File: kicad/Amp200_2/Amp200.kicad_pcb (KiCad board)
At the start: 2 copper layers, 26.2 x 21.9 mm, 38 parts, among them J1 Conn, J10 Conn, J2 Conn, J3 Conn, J5 Conn, J6 Conn, J7 Conn, J8 Conn, J9 Conn, U2 NCP1117-3.3

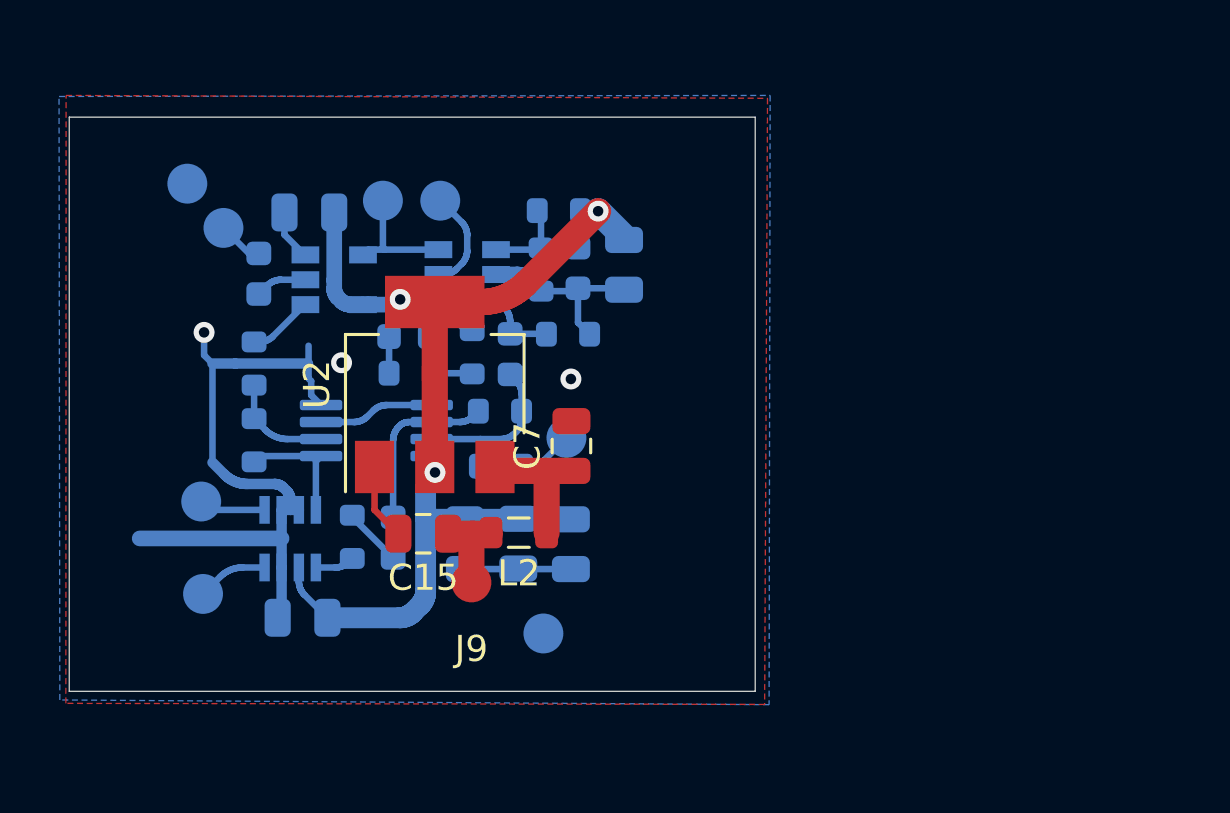
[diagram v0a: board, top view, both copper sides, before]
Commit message: изменено:      kicad/Amp200_2/Amp200-cache.lib 	изменено:      kicad/Amp200_2/Amp200.kicad_pcb 	изменено:      kicad/Amp200_2/Amp200.kicad_pcb-bak 	изменено:      kicad/Amp200_2/Amp200.sch 	изменено:      kicad/Amp200_2/Amp200.sch-bak 	изменено:      kicad/Amp200_2/fp-info-cache 	изменено:      kicad/Anemometr_200_F303/fp-info-cache 	изменено:      stm32cubeide/Anemometer/Release/makefile 	изменено:      stm32cubeide/Anemometer_200_F303/Anemometer_200_F303.ioc 	изменено:      stm32cubeide/Anemometer_200_F303/Core/Inc/main.h 	изменено:      stm32cubeide/Anemometer_200_F303/Core/Inc/stm32f3xx_it.h 	изменено:      stm32cubeide/Anemometer_200_F303/Core/Src/main.c 	изменено:      stm32cubeide/Anemometer_200_F303/Core/Src/stm32f3xx_hal_msp.c 	изменено:      stm32cubeide/Anemometer_200_F303/Core/Src/stm32f3xx_it.c 	изменено:      stm32cubeide/Anemometer_200_F303/Debug/Anemometer_200_F303.bin 	изменено:      stm32cubeide/Anemometer_200_F303/Debug/Anemometer_200_F303.elf 	изменено:      stm32cubeide/Anemometer_200_F303/Debug/Anemometer_200_F303.list 	изменено:      stm32cubeide/Anemometer_200_F303/Debug/Anemometer_200_F303.map 	изменено:      stm32cubeide/Anemometer_200_F303/Debug/Core/Src/main.o 	изменено:      stm32cubeide/Anemometer_200_F303/Debug/Core/Src/main.su 	изменено:      stm32cubeide/Anemometer_200_F303/Debug/Core/Src/stm32f3xx_hal_msp.o 	изменено:      stm32cubeide/Anemometer_200_F303/Debug/Core/Src/stm32f3xx_hal_msp.su 	изменено:      stm32cubeide/Anemometer_200_F303/Debug/Core/Src/stm32f3xx_it.o 	изменено:      stm32cubeide/Anemometer_200_F303/Debug/Core/Src/stm32f3xx_it.su
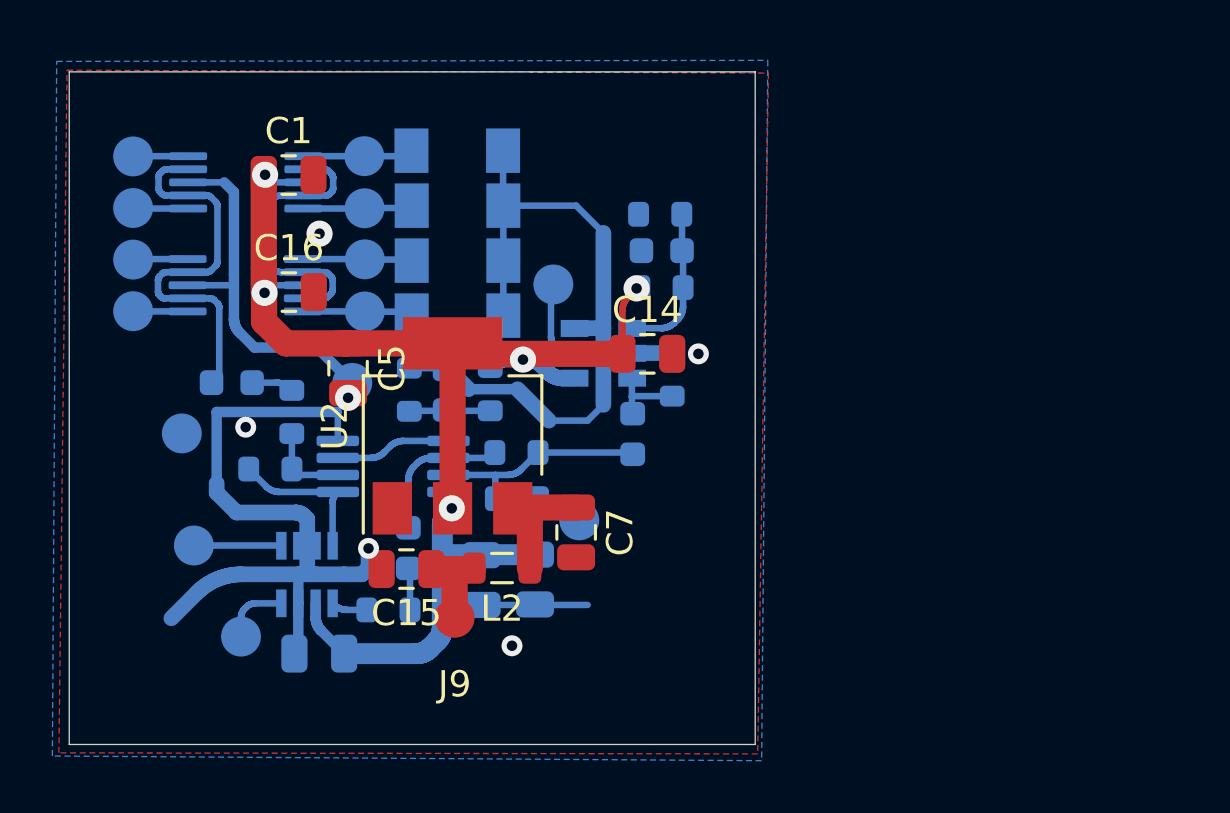
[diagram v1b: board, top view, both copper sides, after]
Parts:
- added C9: 1.5n, Capacitor_SMD:C_0603_1608Metric, B.Cu at (29.1, 47.2)
- added D4: BZ55C2V7, Diode_SMD:D_MiniMELF, B.Cu at (37.7, 44.6)
- added D6: BZ55C2V7, Diode_SMD:D_MiniMELF, B.Cu at (37.7, 40.4)
- added D7: BZ55C2V7, Diode_SMD:D_MiniMELF, B.Cu at (37.7, 38.3)
- added J11: Conn, My-library:SMD-CONN, B.Cu at (34.2, 42.5)
- added J12: Conn, My-library:SMD-CONN, B.Cu at (25.3, 42.5)
- added J13: Conn, My-library:SMD-CONN, B.Cu at (34.2, 40.5)
- added J14: Conn, My-library:SMD-CONN, B.Cu at (25.3, 40.5)
- added J15: Conn, My-library:SMD-CONN, B.Cu at (34.2, 38.5)
- added J16: Conn, My-library:SMD-CONN, B.Cu at (25.3, 38.5)
- added U1: TS5A23159DGS, Package_SO:VSSOP-10_3x3mm_P0.5mm, B.Cu at (29.6, 43.4)
- added U3: TS5A23159DGS, Package_SO:VSSOP-10_3x3mm_P0.5mm, B.Cu at (29.6, 39.5)
- C1: value 1.5n -> .1u; footprint Capacitor_SMD:C_0603_1608Metric -> Capacitor_SMD:C_0805_2012Metric; moved to F.Cu
- C14, C16, C5: moved to F.Cu
- D5: value TS5A4595 -> BZ55C2V7; footprint Package_TO_SOT_SMD:SOT-23-5 -> Diode_SMD:D_MiniMELF
- moved J8 12.0 mm to (33.7, 47.2)
- moved C5 10.8 mm to (33.5, 46.6)
- moved J7 10.4 mm to (25.3, 44.4), turned to 0 degrees
- moved J10 9.54 mm to (27.2, 49.1)
- moved J1 6.27 mm to (34.2, 44.4)
- moved D3 6.01 mm to (43.3, 46.0)
- moved C8 5.59 mm to (44.4, 49.1)
- moved J6 5.38 mm to (41.4, 43.4)
- moved R9 5.02 mm to (45.5, 40.7), turned to 180 degrees
- moved R8 4.90 mm to (45.5, 43.5), turned to 180 degrees
- moved D5 4.77 mm to (37.7, 42.5)
- moved R7 4.27 mm to (45.9, 46.9), turned to 90 degrees
- moved C1 3.94 mm to (31.3, 39.2), turned to 0 degrees
- moved C14 3.51 mm to (45.0, 46.1), turned to 0 degrees
- moved C7 3.30 mm to (42.2, 52.9), turned to 270 degrees
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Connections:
- net Net-(D2-Pad4) renamed /scl
- net Net-(D2-Pad5) renamed /sda
- C1 pad 1: Net-(C1-Pad1) -> /+3.3v
- C1 pad 2: /Input -> GND
- D3 pad 6: /Select -> GND
- D5 pad 1: Net-(D5-Pad1) -> /Z2
- D5 pad 2: Net-(C1-Pad1) -> GND
- J1 pad 1: /Input -> /Z1
- J7 pad 1: /Select -> /Z1sel
- R1 pad 2: Net-(D5-Pad1) -> Net-(C9-Pad1)
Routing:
- net GND: track 42.9 -> 87.7 mm, vias 3 -> 6
- net Net-(C9-Pad2): track 0.00 -> 15.1 mm
- net /+3.3v: track 43.0 -> 51.1 mm, vias 3 -> 5
- net /Select: track 4.86 -> 0.00 mm
- net /Z1: track 0.00 -> 4.23 mm
- net /Z4: track 0.00 -> 4.22 mm
- net /Z3: track 0.00 -> 4.19 mm
- net /Z2: track 0.00 -> 4.18 mm
- net Net-(D5-Pad1): track 2.49 -> 0.00 mm
- net /Z3sel: track 0.00 -> 2.11 mm
- net /Z4sel: track 0.00 -> 2.10 mm
- net /Z2sel: track 0.00 -> 2.09 mm
- net /Z1sel: track 0.00 -> 2.08 mm
- net Net-(C1-Pad1): track 1.94 -> 0.00 mm
- net /Input: track 1.75 -> 0.00 mm
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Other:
- board size 26.2 x 21.9 mm -> 26.2 x 25.7 mm

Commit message: изменено:      kicad/Amp200_2/Amp200-cache.lib 	изменено:      kicad/Amp200_2/Amp200.kicad_pcb 	изменено:      kicad/Amp200_2/Amp200.kicad_pcb-bak 	изменено:      kicad/Amp200_2/Amp200.sch 	изменено:      kicad/Amp200_2/Amp200.sch-bak 	изменено:      kicad/Amp200_2/fp-info-cache 	изменено:      kicad/Anemometr_200_F303/Anemometr_200_F303.kicad_pcb 	изменено:      kicad/Anemometr_200_F303/Anemometr_200_F303.kicad_pcb-bak 	изменено:      kicad/Anemometr_200_F303/Anemometr_200_F303.sch 	изменено:      kicad/Anemometr_200_F303/Anemometr_200_F303.sch-bak 	изменено:      stm32cubeide/Anemometer_200_F303/.cproject 	изменено:      stm32cubeide/Anemometer_200_F303/.mxproject 	изменено:      stm32cubeide/Anemometer_200_F303/.settings/language.settings.xml 	изменено:      stm32cubeide/Anemometer_200_F303/.settings/stm32cubeide.project.prefs 	изменено:      stm32cubeide/Anemometer_200_F303/Anemometer_200_F303.ioc 	изменено:      stm32cubeide/Anemometer_200_F303/Anemometer_200_F303.launch 	изменено:      stm32cubeide/Anemometer_200_F303/Core/Inc/main.h 	изменено:      stm32cubeide/Anemometer_200_F303/Core/Inc/stm32f3xx_hal_conf.h 	изменено:      stm32cubeide/Anemometer_200_F303/Core/Inc/stm32f3xx_it.h 	изменено:      stm32cubeide/Anemometer_200_F303/Core/Src/main.c 	изменено:      stm32cubeide/Anemometer_200_F303/Core/Src/stm32f3xx_hal_msp.c 	изменено:      stm32cubeide/Anemometer_200_F303/Core/Src/stm32f3xx_it.c 	удалено:       stm32cubeide/Anemometer_200_F303/Debug/Anemometer_200_F303.bin 	изменено:      stm32cubeide/Anemometer_200_F303/Debug/Anemometer_200_F303.elf 	изменено:      stm32cubeide/Anemometer_200_F303/Debug/Anemometer_200_F303.list 	изменено:      stm32cubeide/Anemometer_200_F303/Debug/Anemometer_200_F303.map 	изменено:      stm32cubeide/Anemometer_200_F303/Debug/Core/Src/main.d 	изменено:      stm32cubeide/Anemometer_200_F303/Debug/Core/Src/main.o 	изменено:      stm32cubeide/Anemometer_200_F303/Debug/Core/Src/main.su 	изменено:      stm32cubeide/Anemometer_200_F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
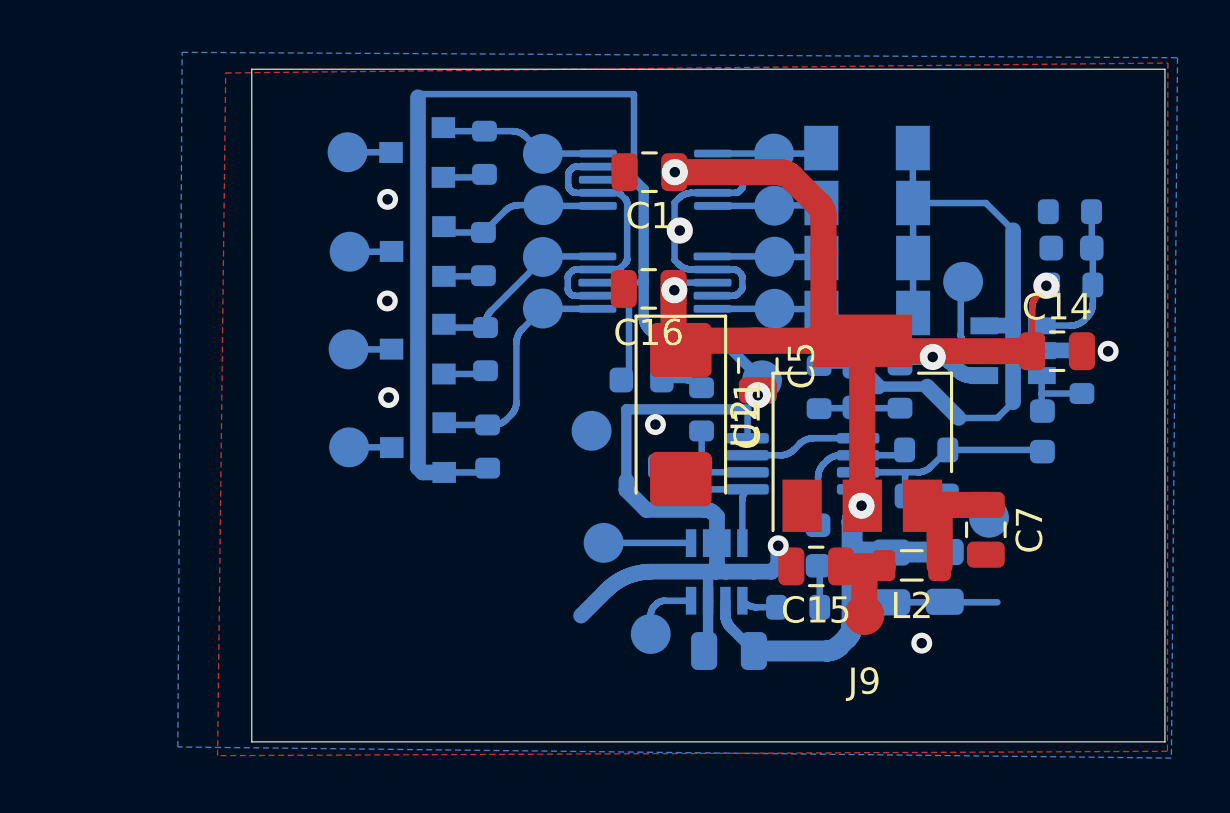
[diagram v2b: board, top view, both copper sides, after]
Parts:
- added C11: CP, Capacitor_Tantalum_SMD:CP_EIA-6032-28_Kemet-C, F.Cu at (46.2, 48.4)
- added J17: Conn, My-library:SMD-CONN, B.Cu at (33.6, 45.9)
- added J18: Conn, My-library:SMD-CONN, B.Cu at (33.5, 38.4)
- added J19: Conn, My-library:SMD-CONN, B.Cu at (41.0, 40.4)
- added J4: Conn, My-library:SMD-CONN, B.Cu at (33.6, 49.6)
- added Q1: Q_NMOS_GSD, Package_TO_SOT_SMD:SOT-23, B.Cu at (36.2, 49.6)
- added Q2: Q_NMOS_GSD, Package_TO_SOT_SMD:SOT-23, B.Cu at (36.2, 45.9)
- added Q3: Q_NMOS_GSD, Package_TO_SOT_SMD:SOT-23, B.Cu at (36.2, 42.1)
- added Q4: Q_NMOS_GSD, Package_TO_SOT_SMD:SOT-23, B.Cu at (36.2, 38.4)
- added R11: 100k, Resistor_SMD:R_0603_1608Metric, B.Cu at (38.9, 49.6)
- added R12: 100k, Resistor_SMD:R_0603_1608Metric, B.Cu at (38.8, 45.9)
- added R13: 100k, Resistor_SMD:R_0603_1608Metric, B.Cu at (38.7, 42.2)
- added R14: 100k, Resistor_SMD:R_0603_1608Metric, B.Cu at (38.8, 38.4)
- moved C13 15.7 mm to (48.1, 57.4)
- moved C8 15.7 mm to (60.1, 49.0)
- moved J15 15.7 mm to (49.8, 38.4)
- moved J5 15.7 mm to (58.0, 52.3)
- moved J10 15.7 mm to (42.8, 49.0)
- moved J2 15.7 mm to (45.1, 56.8)
- moved U3 15.7 mm to (45.3, 39.4)
- moved C10 15.7 mm to (61.2, 42.0)
- moved C14 15.7 mm to (60.6, 46.0)
- moved C15 15.7 mm to (51.4, 54.2)
- moved C2 15.7 mm to (51.5, 53.4)
- moved C3 15.7 mm to (52.9, 47.3)
- moved C4 15.7 mm to (54.3, 54.6)
- moved C5 15.7 mm to (49.2, 46.5)
- moved C6 15.7 mm to (56.3, 54.6)
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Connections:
- J14 pad 1: /Z3sel -> /-Z3
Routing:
- net GND: track 87.7 -> 121.0 mm, vias 6 -> 9
- net /+3.3v: track 51.1 -> 58.9 mm
- net /Z1sel: track 2.08 -> 9.31 mm
- net /Z2sel: track 2.09 -> 7.30 mm
- net /Z3sel: track 2.11 -> 6.40 mm
- net /Z4sel: track 2.10 -> 6.29 mm
- net /-Z4: track 0.00 -> 1.66 mm
- net /-Z2: track 0.00 -> 1.64 mm
- net /-Z1: track 0.00 -> 1.63 mm
- net /-Z3: track 0.00 -> 1.60 mm
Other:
- board size 26.2 x 25.7 mm -> 34.9 x 25.7 mm

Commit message: изменено:      kicad/Amp200_2/Amp200-cache.lib 	изменено:      kicad/Amp200_2/Amp200.kicad_pcb 	изменено:      kicad/Amp200_2/Amp200.kicad_pcb-bak 	изменено:      kicad/Amp200_2/Amp200.sch 	изменено:      kicad/Amp200_2/Amp200.sch-bak
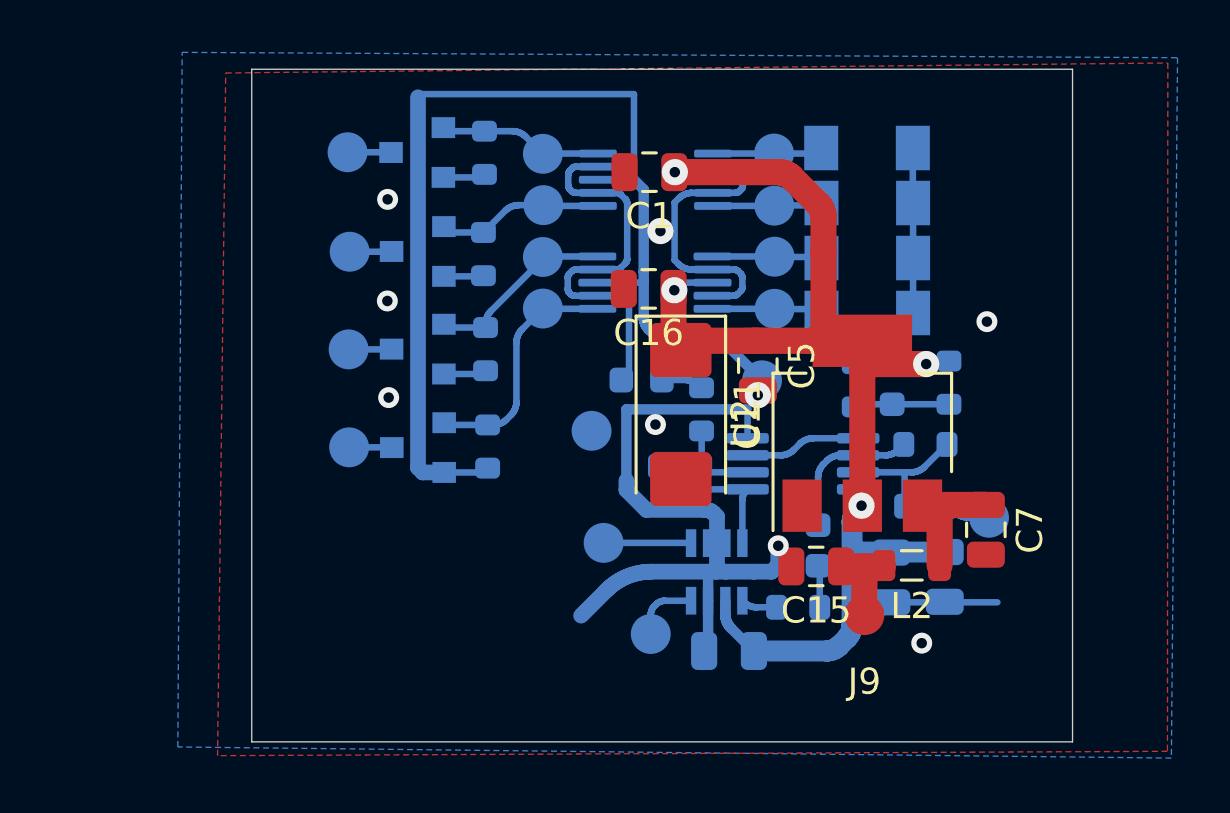
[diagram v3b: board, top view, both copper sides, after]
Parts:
- removed C10: 1u, Capacitor_SMD:C_0603_1608Metric
- removed C14: 1u, Capacitor_SMD:C_0805_2012Metric
- removed C8: 1.5n, Capacitor_SMD:C_0603_1608Metric
- removed D3: TLV3501, Package_TO_SOT_SMD:SOT-23-6
- removed J6: Conn, My-library:SMD-CONN
- removed R7: 10k, Resistor_SMD:R_0603_1608Metric
- removed R8: 100k, Resistor_SMD:R_0603_1608Metric
- removed R9: 5.1k, Resistor_SMD:R_0603_1608Metric
- moved R4 1.88 mm to (56.5, 47.2)
- moved C3 1.43 mm to (54.3, 47.2)
- moved R5 1.34 mm to (52.9, 47.3)
- moved R10 0.39 mm to (55.6, 51.9)
- moved R6 0.21 mm to (55.6, 49.5)
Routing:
- net GND: track 121.0 -> 99.4 mm
- net /+3.3v: track 58.9 -> 50.0 mm, vias 5 -> 4
- net Net-(C10-Pad1): track 5.95 -> 0.00 mm
- net /Zero: track 3.43 -> 0.00 mm
- net Net-(D1-Pad7): track 8.29 -> 5.12 mm
- net Net-(C8-Pad1): track 2.93 -> 0.00 mm
- net Net-(C3-Pad1): track 8.78 -> 9.36 mm
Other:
- board size 34.9 x 25.7 mm -> 31.4 x 25.7 mm

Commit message: изменено:      kicad/Amp200_2/Amp200-cache.lib 	изменено:      kicad/Amp200_2/Amp200-rescue.lib 	изменено:      kicad/Amp200_2/Amp200.kicad_pcb 	изменено:      kicad/Amp200_2/Amp200.kicad_pcb-bak 	изменено:      kicad/Amp200_2/Amp200.sch 	изменено:      kicad/Amp200_2/Amp200.sch-bak 	изменено:      kicad/Amp200_2/sym-lib-table 	изменено:      kicad/Anemometer_200_G473/Anemometer_200_G473-cache.lib 	изменено:      kicad/Anemometer_200_G473/Anemometer_200_G473.sch 	изменено:      kicad/Anemometer_200_G473/Anemometer_200_G473.sch-bak 	изменено:      kicad/Anemometer_200_G473/sym-lib-table
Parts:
- added C8: 470u, Capacitor_Tantalum_SMD:CP_EIA-6032-28_Kemet-C, F.Cu at (50.4, 57.1)
- C11: value CP -> 1000u
- moved C15 3.75 mm to (47.7, 54.0)
- moved J9 2.13 mm to (52.1, 54.3)
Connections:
- net /+12v renamed /+5v
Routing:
- net Net-(C7-Pad1): track 4.80 -> 10.2 mm
- net /+5v: track 3.53 -> 5.45 mm
